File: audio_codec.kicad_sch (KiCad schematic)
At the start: 38 parts, among them J200 Headphones, J201 AudioInput, J202 AudioOutput, U200 WM8731SEDS, U201 TPA6110A2DGN

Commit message: pcb setup
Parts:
- J200: footprint Connector_Audio:Jack_3.5mm_PJ320D_Horizontal -> Galerna:AUDIO-SMD_PJ-320D-1
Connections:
- no-connect marks 10 -> 12
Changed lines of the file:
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@@
 	)
 	(no_connect
+		(at 99.06 223.52)
+	)
+	(no_connect
 		(at 292.1 86.36)
 	)
 	(no_connect
+		(at 99.06 208.28)
+	)
+	(no_connect
 		(at 107.95 69.85)
 	)
@@
 				)
 			)
+			(project "audio_codec"
+				(path "/e3b3de50-cc7b-41ec-a880-fcc1cb4fca88"
+					(reference "#FLG?")
+					(unit 1)
+				)
+			)
 		)
 	)
@@
 		(pin "1"
 		)
+		(pin "6"
+		)
+		(pin "7"
+		)
 		(instances
 			(project "GalernaDsp"
@@
 			)
 		)
-		(property "Footprint" "Connector_Audio:Jack_3.5mm_PJ320D_Horizontal"
+		(property "Footprint" "Galerna:AUDIO-SMD_PJ-320D-1"
 			(at 295.91 106.68 0)
 			(effects

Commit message: codec placed
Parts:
- removed C212, C213: 100u, Capacitor_SMD:C_0603_1608Metric, symbol Device:C
- added C212, C213: 100u, Galerna:CHEMI-F80, symbol Device:C_Polarized
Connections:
- net HEADPHONE_OUT_L: now also C212.2
- net HEADPHONE_OUT_R: now also C213.2
- net at R203.2, U201.5 (VO2): now also C213.1
- net at R202.2, U201.7 (VO1): now also C212.1
- net I2S_SCA renamed I2C_SDA
- net I2S_SCL renamed I2C_SCL
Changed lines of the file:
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@@
 		)
 	)
-	(global_label "I2S_SCA"
+	(global_label "I2C_SDA"
 		(shape input)
 		(at 85.09 90.17 180)
@@
 		)
 		(property "Intersheetrefs" "${INTERSHEET_REFS}"
-			(at 74.5453 90.17 0)
+			(at 74.4848 90.17 0)
 			(effects
 				(font
@@
 		)
 	)
-	(global_label "I2S_SCL"
+	(global_label "I2C_SCL"
 		(shape input)
 		(at 85.09 92.71 180)
@@
 		)
 		(property "Intersheetrefs" "${INTERSHEET_REFS}"
-			(at 74.6058 92.71 0)
+			(at 74.5453 92.71 0)
 			(effects
 				(font
@@
 	)
 	(symbol
+		(lib_id "Device:C_Polarized")
+		(at 187.96 217.17 90)
+		(unit 1)
+		(exclude_from_sim no)
+		(in_bom yes)
+		(on_board yes)
+		(dnp no)
+		(property "Reference" "C213"
+			(at 188.214 222.504 90)
+			(effects
+				(font
+					(size 1.27 1.27)
+				)
+			)
+		)
+		(property "Value" "100u"
+			(at 188.214 225.044 90)
+			(effects
+				(font
+					(size 1.27 1.27)
+				)
+			)
+		)
+		(property "Footprint" "Galerna:CHEMI-F80"
+			(at 191.77 216.2048 0)
+			(effects
+				(font
+					(size 1.27 1.27)
+				)
+			)
+		)
+		(property "Datasheet" "~"
+			(at 187.96 217.17 0)
+			(effects
+				(font
+					(size 1.27 1.27)
+				)
+				(hide yes)
+			)
+		)
+		(property "Description" "Polarized capacitor"
+			(at 187.96 217.17 0)
+			(effects
+				(font
+					(size 1.27 1.27)
+				)
+				(hide yes)
+			)
+		)
+		(pin "1"
+		)
+		(pin "2"
+		)
+		(instances
+			(project "GalernaDsp"
+				(path "/a77f8f1b-3e6d-40f9-a36e-54a20299e9bc/c8eca522-3096-4cb1-b457-c66eaba9f73c"
+					(reference "C213")
+					(unit 1)
+				)
+			)
+		)
+	)
+	(symbol
 		(lib_id "Device:R")
 		(at 213.36 96.52 90)
@@
 	)
 	(symbol
+		(lib_id "Device:C_Polarized")
+		(at 187.96 212.09 90)
+		(unit 1)
+		(exclude_from_sim no)
+		(in_bom yes)
+		(on_board yes)
+		(dnp no)
+		(fields_autoplaced yes)
+		(property "Reference" "C212"
+			(at 187.071 204.47 90)
+			(effects
+				(font
+					(size 1.27 1.27)
+				)
+			)
+		)
+		(property "Value" "100u"
+			(at 187.071 207.01 90)
+			(effects
+				(font
+					(size 1.27 1.27)
+				)
+			)
+		)
+		(property "Footprint" "Galerna:CHEMI-F80"
+			(at 191.77 211.1248 0)
+			(effects
+				(font
+					(size 1.27 1.27)
+				)
+				(hide yes)
+			)
+		)
+		(property "Datasheet" "~"
+			(at 187.96 212.09 0)
+			(effects
+				(font
+					(size 1.27 1.27)
+				)
+				(hide yes)
+			)
+		)
+		(property "Description" "Polarized capacitor"
+			(at 187.96 212.09 0)
+			(effects
+				(font
+					(size 1.27 1.27)
+				)
+				(hide yes)
+			)
+		)
+		(pin "1"
+		)
+		(pin "2"
+		)
+		(instances
+			(project ""
+				(path "/a77f8f1b-3e6d-40f9-a36e-54a20299e9bc/c8eca522-3096-4cb1-b457-c66eaba9f73c"
+					(reference "C212")
+					(unit 1)
+				)
+			)
+		)
+	)
+	(symbol
 		(lib_id "power:GND")
 		(at 146.05 129.54 0)
@@
 	(symbol
 		(lib_id "Device:C")
-		(at 187.96 212.09 90)
-		(unit 1)
-		(exclude_from_sim no)
-		(in_bom yes)
-		(on_board yes)
-		(dnp no)
-		(property "Reference" "C212"
-			(at 187.96 208.28 90)
-			(effects
-				(font
-					(size 1.27 1.27)
-				)
-			)
-		)
-		(property "Value" "100u"
-			(at 192.024 210.312 90)
-			(effects
-				(font
-					(size 1.27 1.27)
-				)
-			)
-		)
-		(property "Footprint" "Capacitor_SMD:C_0603_1608Metric"
-			(at 191.77 211.1248 0)
-			(effects
-				(font
-					(size 1.27 1.27)
-				)
-				(hide yes)
-			)
-		)
-		(property "Datasheet" "~"
-			(at 187.96 212.09 0)
-			(effects
-				(font
-					(size 1.27 1.27)
-				)
-				(hide yes)
-			)
-		)
-		(property "Description" "Unpolarized capacitor"
-			(at 187.96 212.09 0)
-			(effects
-				(font
-					(size 1.27 1.27)
-				)
-				(hide yes)
-			)
-		)
-		(pin "1"
-		)
-		(pin "2"
-		)
-		(instances
-			(project "GalernaDsp"
-				(path "/a77f8f1b-3e6d-40f9-a36e-54a20299e9bc/c8eca522-3096-4cb1-b457-c66eaba9f73c"
-					(reference "C212")
-					(unit 1)
-				)
-			)
-			(project ""
-				(path "/e3b3de50-cc7b-41ec-a880-fcc1cb4fca88"
-					(reference "C5")
-					(unit 1)
-				)
-			)
-		)
-	)
-	(symbol
-		(lib_id "Device:C")
 		(at 58.42 58.42 0)
 		(unit 1)
@@
 					(unit 1)
 				)
-			)
-		)
-	)
-	(symbol
-		(lib_id "Device:C")
-		(at 187.96 217.17 90)
-		(unit 1)
-		(exclude_from_sim no)
-		(in_bom yes)
-		(on_board yes)
-		(dnp no)
-		(property "Reference" "C213"
-			(at 187.96 221.234 90)
-			(effects
-				(font
-					(size 1.27 1.27)
-				)
-			)
-		)
-		(property "Value" "100u"
-			(at 191.77 219.202 90)
-			(effects
-				(font
-					(size 1.27 1.27)
-				)
-			)
-		)
-		(property "Footprint" "Capacitor_SMD:C_0603_1608Metric"
-			(at 191.77 216.2048 0)
-			(effects
-				(font
-					(size 1.27 1.27)
-				)
-				(hide yes)
-			)
-		)
-		(property "Datasheet" "~"
-			(at 187.96 217.17 0)
-			(effects
-				(font
-					(size 1.27 1.27)
-				)
-				(hide yes)
-			)
-		)
-		(property "Description" "Unpolarized capacitor"
-			(at 187.96 217.17 0)
-			(effects
-				(font
-					(size 1.27 1.27)
-				)
-				(hide yes)
-			)
-		)
-		(pin "1"
-		)
-		(pin "2"
-		)
-		(instances
-			(project "GalernaDsp"
-				(path "/a77f8f1b-3e6d-40f9-a36e-54a20299e9bc/c8eca522-3096-4cb1-b457-c66eaba9f73c"
-					(reference "C213")
-					(unit 1)
-				)
-			)
-			(project "audio_codec"
-				(path "/e3b3de50-cc7b-41ec-a880-fcc1cb4fca88"
-					(reference "C6")
-					(unit 1)
-				)

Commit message: control positioned
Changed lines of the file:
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@@
 					(size 1.27 1.27)
 				)
+				(hide yes)
 			)
 		)

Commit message: updating names
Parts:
- removed VolumeControlKnob200: ~, Galerna:RK10J12R0A0B, symbol Galerna:RK10J12R0A0B
- added R212: RK09L12D0A1W, Galerna:RK09L12D0A1W_AAL, symbol Galerna:RK09L12D0A1W
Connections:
- net AUDIO_L_OUT: now also R212.6
- net AUDIO_R_OUT: now also R212.3
- net AUDIO_WIPER_OUT_L: now also R212.5
- net AUDIO_WIPER_OUT_R: now also R212.2
- net GND: now also R212.1, R212.4
- net I2C_SCL renamed CODEC_I2C_SCL
- net I2C_SDA renamed CODEC_I2C_SDA
- net I2S_CK renamed CODEC_I2S_CK
- net I2S_MCK renamed CODEC_I2S_MCK
- net I2S_SD renamed CODEC_I2S_SD
- net I2S_SDI renamed CODEC_I2S_SDI
- net I2S_WS renamed CODEC_I2S_WS
- no-connect marks 12 -> 10

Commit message: routing update
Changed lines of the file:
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@@
 	)
 	(global_label "CODEC_I2S_SDI"
-		(shape input)
+		(shape output)
 		(at 85.09 80.01 180)
 		(fields_autoplaced yes)
@@
 	)
 	(global_label "CODEC_I2C_SDA"
-		(shape input)
+		(shape bidirectional)
 		(at 85.09 90.17 180)
 		(fields_autoplaced yes)
@@
 		)
 		(property "Intersheetrefs" "${INTERSHEET_REFS}"
-			(at 67.2277 90.17 0)
+			(at 66.1164 90.17 0)
 			(effects
 				(font

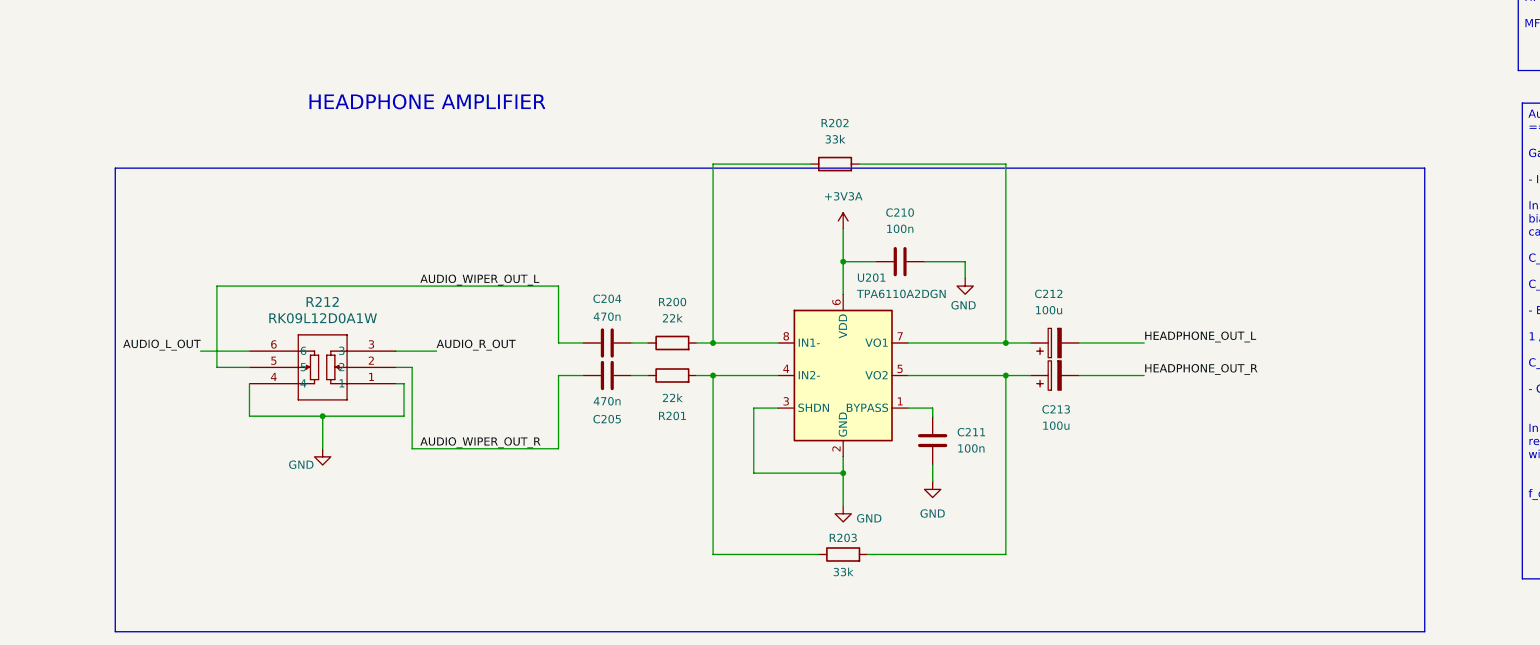
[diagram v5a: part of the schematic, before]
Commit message: headphone amplifier routing
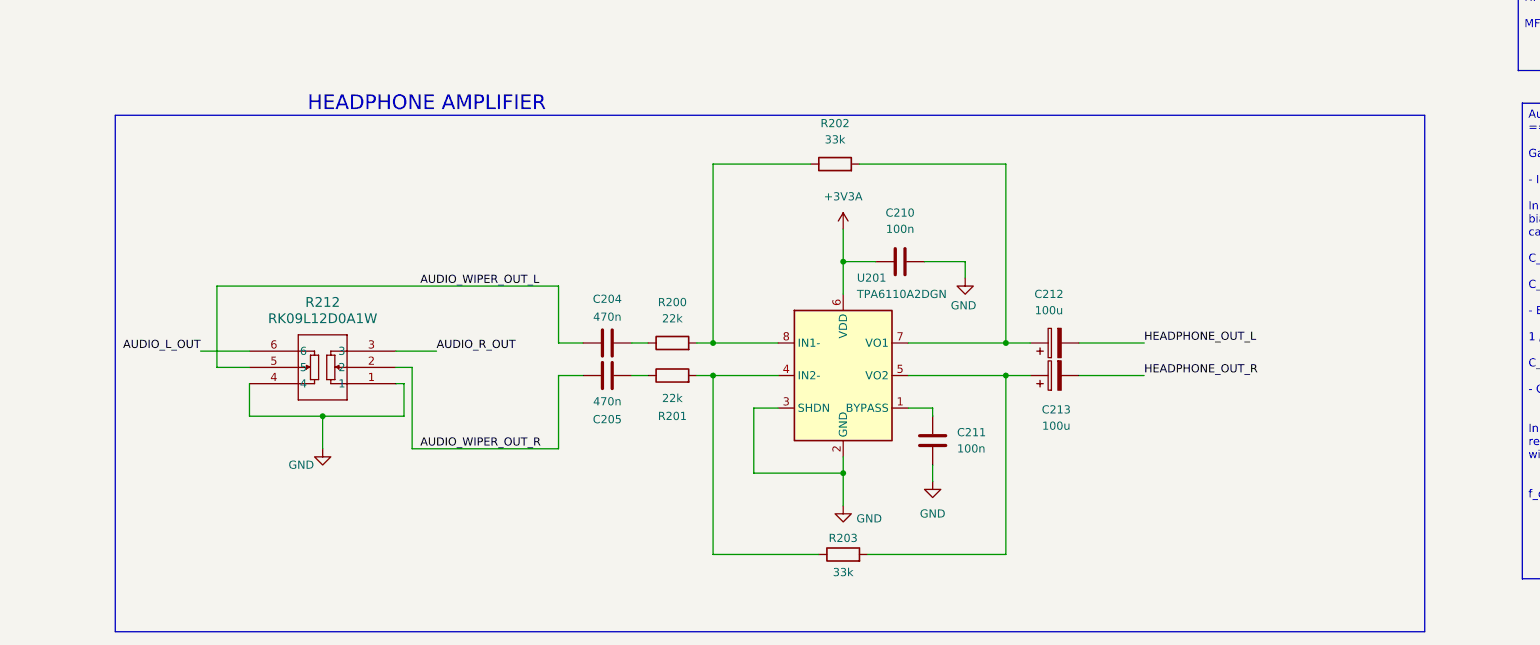
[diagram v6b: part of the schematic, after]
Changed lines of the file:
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@@
 	)
 	(rectangle
-		(start 41.275 184.785)
+		(start 41.275 176.53)
 		(end 245.745 257.175)
 		(stroke

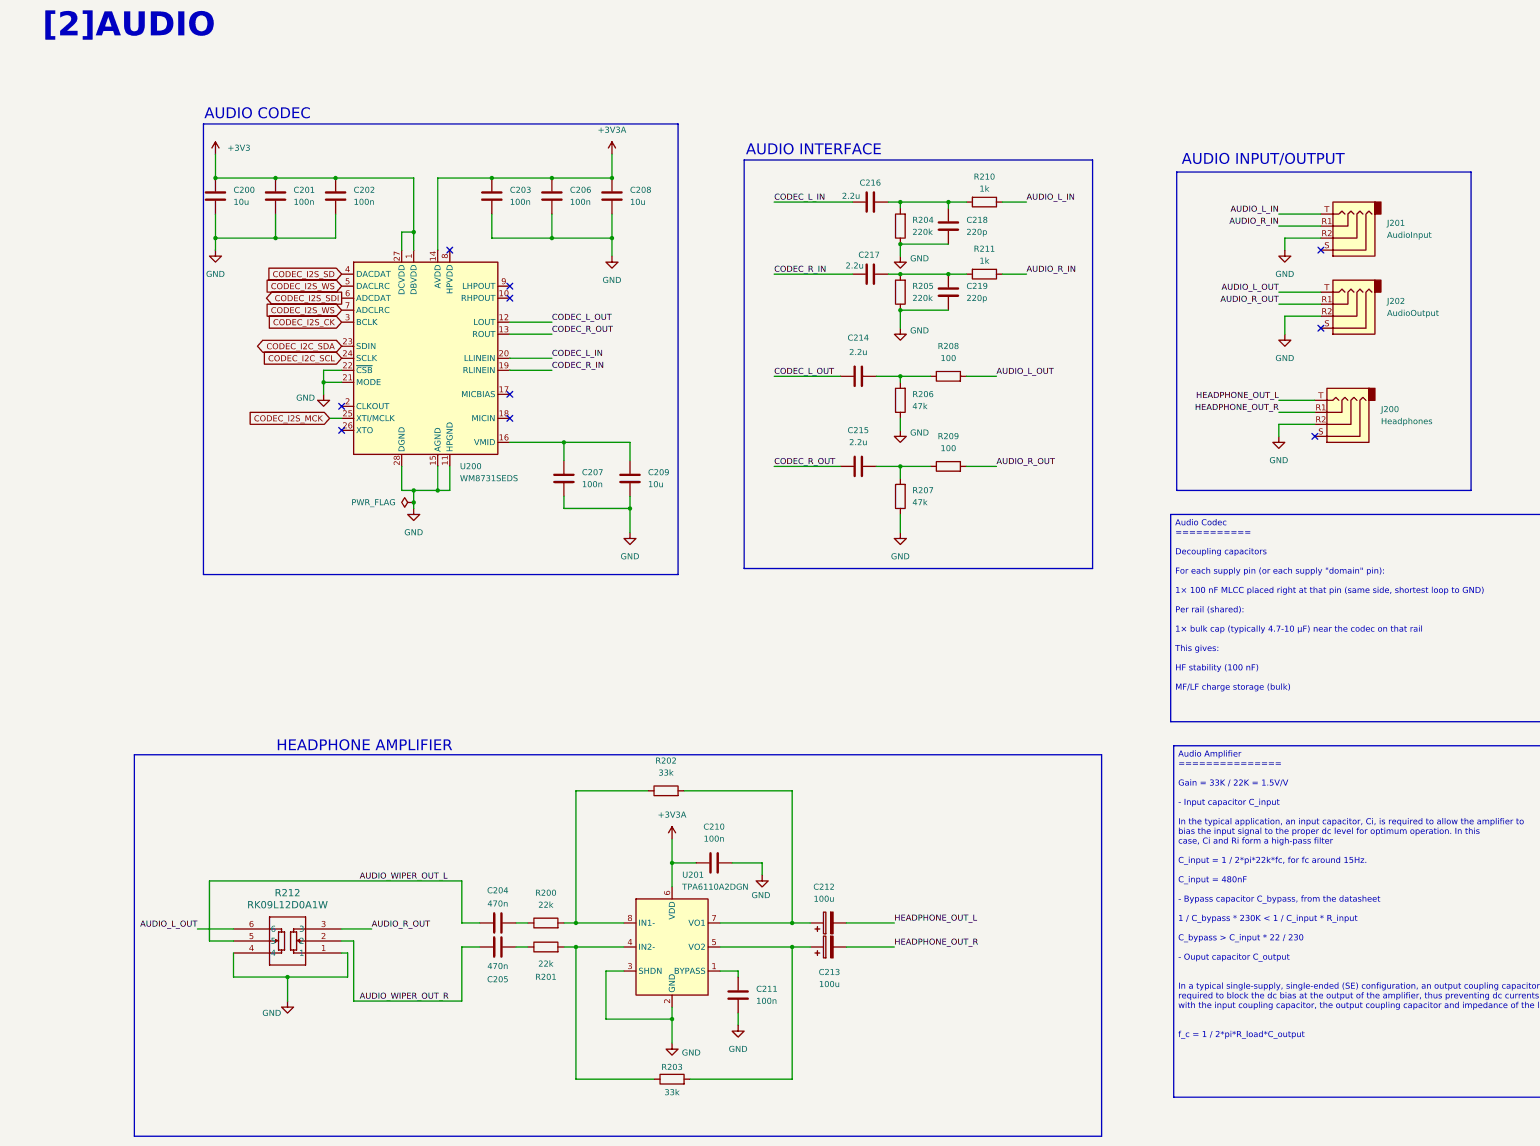
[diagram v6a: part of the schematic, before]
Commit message: Codec updated to ES8388 on schematic
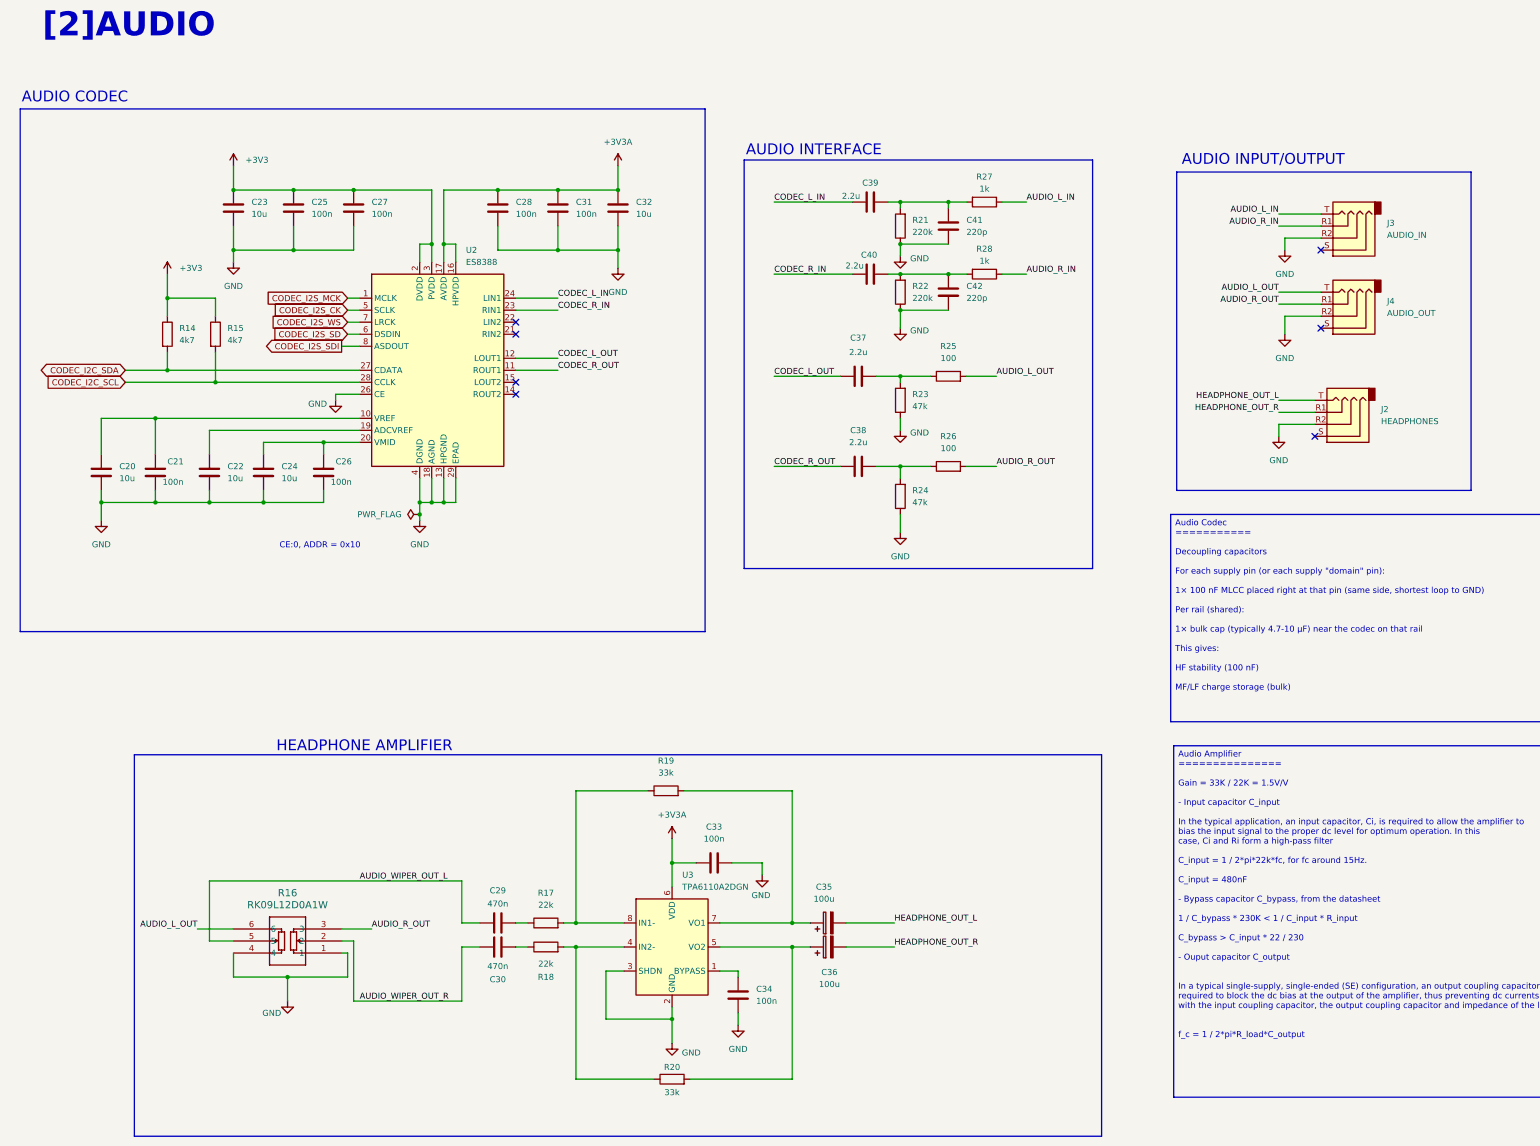
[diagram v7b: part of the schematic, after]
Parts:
- removed C200, C209: 10u, Capacitor_SMD:C_0603_1608Metric, symbol Device:C
- removed C201, C202, C207: 100n, Capacitor_SMD:C_0402_1005Metric, symbol Device:C
- removed U200: WM8731SEDS, Package_SO:SSOP-28_5.3x10.2mm_P0.65mm, symbol Audio:WM8731SEDS
- added C20, C22, C23, C24: 10u, Capacitor_SMD:C_0603_1608Metric, symbol Device:C
- added C21, C26: 100n, Capacitor_SMD:C_0603_1608Metric, symbol Device:C
- added C25, C27: 100n, Capacitor_SMD:C_0402_1005Metric, symbol Device:C
- added R14, R15: 4k7, symbol Device:R
- added U2: ES8388, Package_DFN_QFN:QFN-28-1EP_4x4mm_P0.45mm_EP2.6x2.6mm, symbol Audio:ES8388
- J2: renamed from J200; value Headphones -> HEADPHONES
- J3: renamed from J201; value AudioInput -> AUDIO_IN
- J4: renamed from J202; value AudioOutput -> AUDIO_OUT
- renumbered C203 to C28, C204 to C29, C205 to C30, C206 to C31, C208 to C32, C210 to C33, C211 to C34, C212 to C35, C213 to C36, C214 to C37, C215 to C38, C216 to C39, C217 to C40, C218 to C41, C219 to C42, R212 to R16, R200 to R17, R201 to R18, R202 to R19, R203 to R20, R204 to R21, R205 to R22, R206 to R23, R207 to R24, R208 to R25, R209 to R26, R210 to R27, R211 to R28, U201 to U3
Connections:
- net +3V3: now also C23.1, C25.1, C27.1, R14.1, R15.1, U2.2 (DVDD), U2.3 (PVDD)
- net +3V3A: now also U2.16 (HPVDD), U2.17 (AVDD)
- net CODEC_I2C_SCL: now also R15.2, U2.28 (CCLK)
- net CODEC_I2C_SDA: now also R14.2, U2.27 (CDATA)
- net CODEC_I2S_CK: now also U2.5 (SCLK)
- net CODEC_I2S_MCK: now also U2.1 (MCLK)
- net CODEC_I2S_SD: now also U2.6 (DSDIN)
- net CODEC_I2S_SDI: now also U2.8 (ASDOUT)
- net CODEC_I2S_WS: now also U2.7 (LRCK)
- net CODEC_L_IN: now also U2.24 (LIN1)
- net CODEC_L_OUT: now also U2.12 (LOUT1)
- net CODEC_R_IN: now also U2.23 (RIN1)
- net CODEC_R_OUT: now also U2.11 (ROUT1)
- net GND: now also C20.2, C21.2, C22.2, C23.2, C24.2, C25.2, C26.2, C27.2, U2.13 (HPGND), U2.18 (AGND), U2.26 (CE), U2.29 (EPAD), U2.4 (DGND)
- new net: C20.1, C21.1, U2.10 (VREF)
- new net: C24.1, C26.1, U2.20 (VMID)
- new net: C22.1, U2.19 (ADCVREF)
- no-connect marks 10 -> 7
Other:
- note added: "CE:0, ADDR = 0x10"
- moved on the sheet: C28, C31, C32

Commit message: ES8388 placed
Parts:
- U2: footprint Package_DFN_QFN:QFN-28-1EP_4x4mm_P0.45mm_EP2.6x2.6mm -> Galerna:ES8388
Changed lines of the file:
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@@
 	)
 	(junction
+		(at 58.42 97.79)
+		(diameter 0)
+		(color 0 0 0 0)
+	)
+	(junction
 		(at 62.23 69.85)
 		(diameter 0)
@@
 	)
 	(junction
-		(at 58.42 97.79)
-		(diameter 0)
-		(color 0 0 0 0)
-	)
-	(junction
 		(at 101.6 125.73)
 		(diameter 0)
@@
 	)
 	(junction
-		(at 74.93 57.15)
+		(at 154.94 232.41)
 		(diameter 0)
 		(color 0 0 0 0)
 	)
 	(junction
-		(at 154.94 232.41)
+		(at 74.93 57.15)
 		(diameter 0)
 		(color 0 0 0 0)
@@
 	(wire
 		(pts
+			(xy 39.37 97.79) (xy 58.42 97.79)
+		)
+		(stroke
+			(width 0)
+			(type default)
+		)
+	)
+	(wire
+		(pts
 			(xy 203.2 59.69) (xy 203.2 60.96)
 		)
@@
 	(wire
 		(pts
-			(xy 39.37 97.79) (xy 58.42 97.79)
-		)
-		(stroke
-			(width 0)
-			(type default)
-		)
-	)
-	(wire
-		(pts
 			(xy 85.09 215.9) (xy 87.63 215.9)
 		)
@@
 	(wire
 		(pts
-			(xy 74.93 57.15) (xy 87.63 57.15)
-		)
-		(stroke
-			(width 0)
-			(type default)
-		)
-	)
-	(wire
-		(pts
 			(xy 87.63 215.9) (xy 87.63 228.6)
 		)
@@
 	(wire
 		(pts
+			(xy 74.93 57.15) (xy 87.63 57.15)
+		)
+		(stroke
+			(width 0)
+			(type default)
+		)
+	)
+	(wire
+		(pts
 			(xy 45.72 105.41) (xy 45.72 113.03)
 		)
@@
 	(wire
 		(pts
+			(xy 39.37 95.25) (xy 48.26 95.25)
+		)
+		(stroke
+			(width 0)
+			(type default)
+		)
+	)
+	(wire
+		(pts
 			(xy 217.17 115.57) (xy 223.52 115.57)
 		)
@@
 	(wire
 		(pts
-			(xy 39.37 95.25) (xy 48.26 95.25)
-		)
-		(stroke
-			(width 0)
-			(type default)
-		)
-	)
-	(wire
-		(pts
 			(xy 292.1 67.31) (xy 284.48 67.31)
 		)
@@
 			)
 		)
-		(property "Footprint" "Package_DFN_QFN:QFN-28-1EP_4x4mm_P0.45mm_EP2.6x2.6mm"
+		(property "Footprint" "Galerna:ES8388"
 			(at 106.68 128.27 0)
 			(effects
